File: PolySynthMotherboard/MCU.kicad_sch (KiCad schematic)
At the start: 45 parts, among them J201 SWD Header, J202 USB_C_Leceptacle_USB2.0, J203 MIDI_In, J204 MIDI_Thru, J205 MIDI_Out, J401 Micro_SD_Card_Det2, SW201 RST, SW202 BOOT, U201 STM32F411RETx, U202 74HC595, U203 74HC595, U204 4N35, U205 74HC04, Y201 16MHz, Y202 32.768kHZ

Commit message: power supply tweaks
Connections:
- net BATT_REF: now also U201.14 (PA0); no longer U201.26 (PB0)
- new net DAC_INH: U201.26 (PB0)
- no-connect marks 25 -> 24
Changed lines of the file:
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@@
   (no_connect (at 200.406 137.414))
   (no_connect (at 121.158 55.118))
-  (no_connect (at 121.158 47.498))
   (no_connect (at 185.928 212.852))
   (no_connect (at 121.158 62.738))
@@
   )
   (wire (pts (xy 115.57 31.242) (xy 115.57 32.004))
+    (stroke (width 0) (type default))
+  )
+  (wire (pts (xy 121.158 47.498) (xy 124.714 47.498))
     (stroke (width 0) (type default))
   )
@@
     )
   )
+  (global_label "DAC_INH" (shape output) (at 126.873 90.678 0) (fields_autoplaced)
+    (effects (font (size 1.27 1.27)) (justify left))
+    (property "Intersheetrefs" "${INTERSHEET_REFS}" (at 137.7202 90.678 0)
+      (effects (font (size 1.27 1.27)) (justify left) hide)
+    )
+  )
   (global_label "MIDI_LX" (shape output) (at 384.937 47.244 0) (fields_autoplaced)
     (effects (font (size 1.27 1.27)) (justify left))
@@
     )
   )
-  (global_label "BATT_REF" (shape input) (at 126.873 90.678 0) (fields_autoplaced)
-    (effects (font (size 1.27 1.27)) (justify left))
-    (property "Intersheetrefs" "${INTERSHEET_REFS}" (at 138.6272 90.678 0)
-      (effects (font (size 1.27 1.27)) (justify left) hide)
-    )
+  (global_label "BATT_REF" (shape input) (at 124.714 47.498 0) (fields_autoplaced)
+    (effects (font (size 1.27 1.27)) (justify left))
+    (property "Intersheetrefs" "${INTERSHEET_REFS}" (at 136.4682 47.498 0)
+      (effects (font (size 1.27 1.27)) (justify left) hide)
+    )

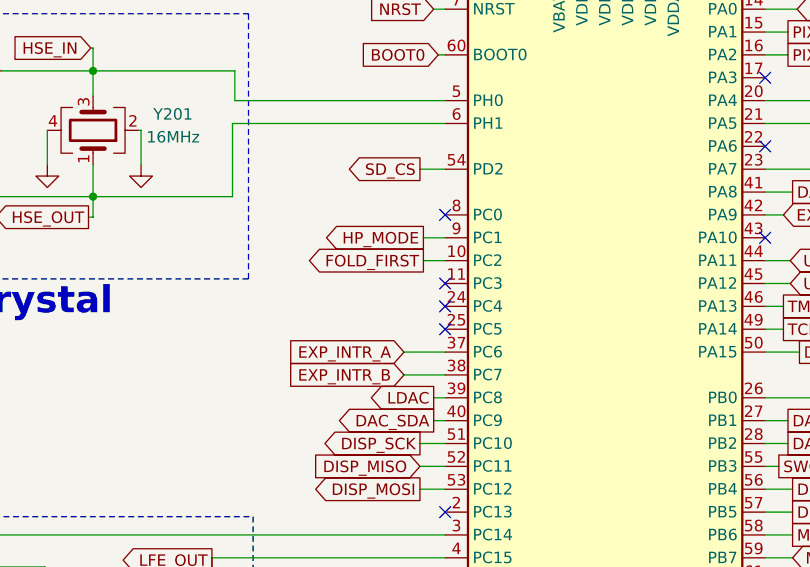
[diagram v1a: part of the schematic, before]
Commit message: cleaned up CV opamps
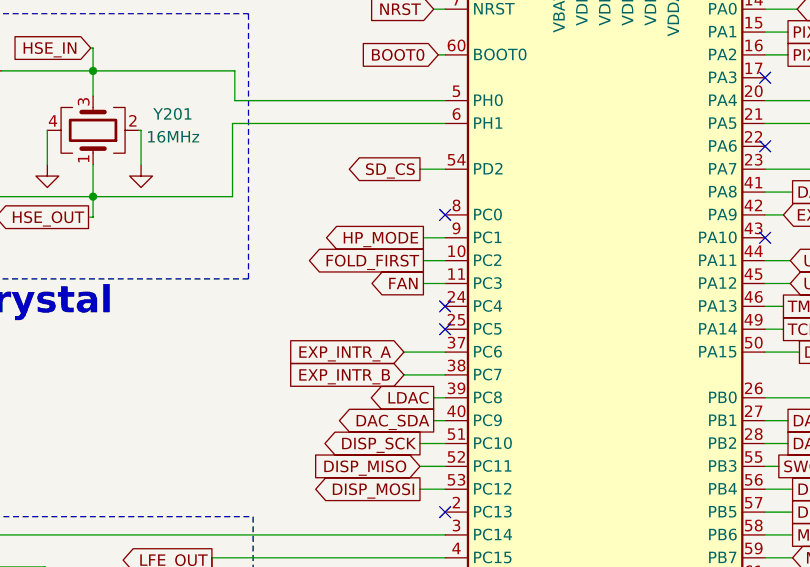
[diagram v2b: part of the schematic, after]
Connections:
- net FAN: now reaches U201.11 (PC3)
- no-connect marks 24 -> 23
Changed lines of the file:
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@@
   (no_connect (at 85.598 70.358))
   (no_connect (at 121.158 72.898))
-  (no_connect (at 85.598 77.978))
   (no_connect (at 279.654 65.659))
   (no_connect (at 85.598 103.378))
@@
     (stroke (width 0) (type default))
   )
+  (wire (pts (xy 83.185 77.978) (xy 85.598 77.978))
+    (stroke (width 0) (type default))
+  )
   (wire (pts (xy 308.102 58.547) (xy 308.102 63.119))
     (stroke (width 0) (type default))
@@
     )
   )
+  (global_label "FAN" (shape output) (at 83.185 77.978 180) (fields_autoplaced)
+    (effects (font (size 1.27 1.27)) (justify right))
+    (property "Intersheetrefs" "${INTERSHEET_REFS}" (at 76.6921 77.978 0)
+      (effects (font (size 1.27 1.27)) (justify right) hide)
+    )
+  )

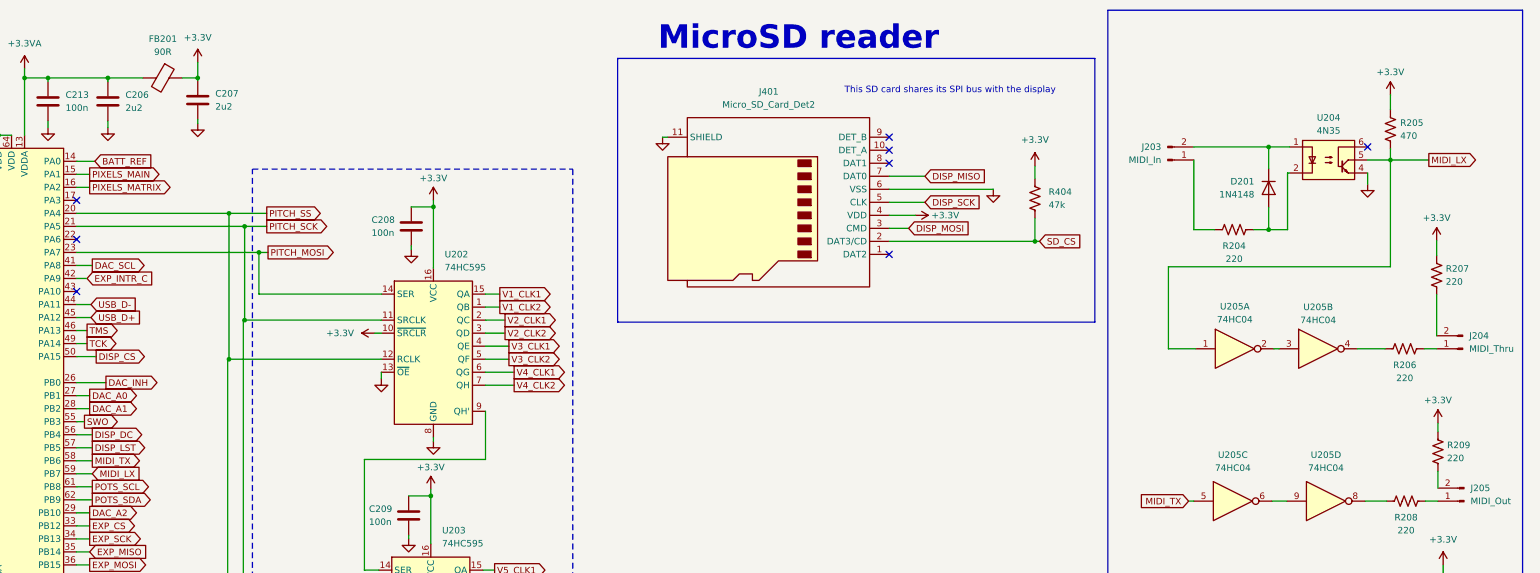
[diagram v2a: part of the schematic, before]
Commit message: footprints placed
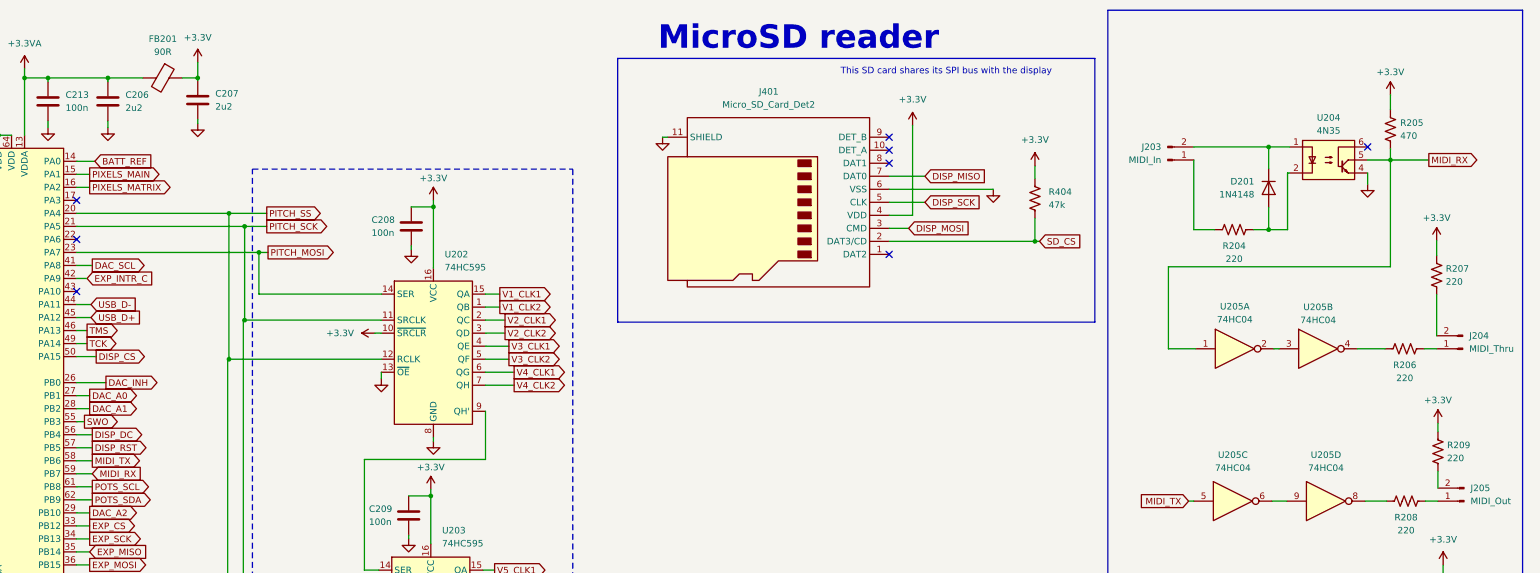
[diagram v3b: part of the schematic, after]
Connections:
- net DISP_LST renamed DISP_RST
- net MIDI_LX renamed MIDI_RX
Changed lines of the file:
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@@
+    (stroke (width 0) (type default))
+  )
+  (wire (pts (xy 284.226 40.513) (xy 284.226 58.039))
     (stroke (width 0) (type default))
   )
@@
     (stroke (width 0) (type default))
   )
+  (wire (pts (xy 284.226 58.039) (xy 279.654 58.039))
+    (stroke (width 0) (type default))
+  )
   (wire (pts (xy 200.914 86.106) (xy 205.486 86.106))
     (stroke (width 0) (type default))
@@
   )
   (wire (pts (xy 190.754 56.388) (xy 190.754 68.326))
-    (stroke (width 0) (type default))
-  )
-  (wire (pts (xy 279.654 58.039) (xy 284.734 58.039))
     (stroke (width 0) (type default))
   )
@@
     (effects (font (size 3 3) (thickness 0.6) bold) (justify left bottom))
   )
-  (text "This SD card shares its SPI bus with the display" (at 312.166 34.417 0)
+  (text "This SD card shares its SPI bus with the display" (at 311.404 30.734 0)
     (effects (font (size 1.27 1.27)) (justify right bottom))
   )
@@
     )
   )
-  (global_label "MIDI_LX" (shape input) (at 124.206 108.458 0) (fields_autoplaced)
+  (global_label "MIDI_RX" (shape input) (at 124.206 108.458 0) (fields_autoplaced)
     (effects (font (size 1.27 1.27)) (justify left))
     (property "Intersheetrefs" "${INTERSHEET_REFS}" (at 134.5693 108.458 0)
@@
     )
   )
-  (global_label "MIDI_LX" (shape output) (at 384.937 47.244 0) (fields_autoplaced)
+  (global_label "MIDI_RX" (shape output) (at 384.937 47.244 0) (fields_autoplaced)
     (effects (font (size 1.27 1.27)) (justify left))
     (property "Intersheetrefs" "${INTERSHEET_REFS}" (at 395.3003 47.244 0)
@@
     )
   )
-  (global_label "DISP_LST" (shape output) (at 124.206 103.378 0) (fields_autoplaced)
+  (global_label "DISP_RST" (shape output) (at 124.206 103.378 0) (fields_autoplaced)
     (effects (font (size 1.27 1.27)) (justify left))
     (property "Intersheetrefs" "${INTERSHEET_REFS}" (at 135.9602 103.378 0)
@@
     )
   )
+  (symbol (lib_id "power:+3.3V") (at 284.226 40.513 0) (unit 1)
+    (in_bom yes) (on_board yes) (dnp no) (fields_autoplaced)
+    (property "Reference" "#PWR0425" (at 284.226 44.323 0)
+      (effects (font (size 1.27 1.27)) hide)
+    )
+    (property "Value" "+3.3V" (at 284.226 35.433 0)
+      (effects (font (size 1.27 1.27)))
+    )
+    (property "Footprint" "" (at 284.226 40.513 0)
+      (effects (font (size 1.27 1.27)) hide)
+    )
+    (property "Datasheet" "" (at 284.226 40.513 0)
+      (effects (font (size 1.27 1.27)) hide)
+    )
+    (pin "1")
+    (instances
+      (project "ESP808_mk3"
+        (path "/1b0f4827-7224-4696-9105-e83073878432/12afefba-537f-4d88-bb0b-d3898664142d"
+          (reference "#PWR0425") (unit 1)
+        )
+      )
+      (project "PolySynthMotherboard"
+        (path "/22649217-9810-470f-bc7b-6f743ad2b90e/30ed774f-a7f6-4caf-bf27-d83abb3db248"
+          (reference "#PWR0249") (unit 1)
+        )
+      )
+      (project "Quadriscope"
+        (path "/b6082534-8496-42f5-914d-c32eba9832ab"
+          (reference "#PWR0164") (unit 1)
+        )
+      )
+      (project "MCU"
+        (path "/dbce208f-32c5-4e57-807b-6eb4ab6aa944"
+          (reference "#PWR0425") (unit 1)
+        )
+      )
+    )
+  )
   (symbol (lib_id "Connector:Micro_SD_Card_Det2") (at 256.794 55.499 180) (unit 1)
     (in_bom yes) (on_board yes) (dnp no) (fields_autoplaced)
@@
         )
       )
-    )
-  )
-  (symbol (lib_id "power:+3.3V") (at 284.734 58.039 270) (unit 1)
-    (in_bom yes) (on_board yes) (dnp no) (fields_autoplaced)
-    (property "Reference" "#PWR0411" (at 280.924 58.039 0)
-      (effects (font (size 1.27 1.27)) hide)
-    )
-    (property "Value" "+3.3V" (at 287.909 58.039 90)
-      (effects (font (size 1.27 1.27)) (justify left))
-    )
-    (property "Footprint" "" (at 284.734 58.039 0)
-      (effects (font (size 1.27 1.27)) hide)
-    )
-    (property "Datasheet" "" (at 284.734 58.039 0)
-      (effects (font (size 1.27 1.27)) hide)
-    )
-    (pin "1")
-    (instances
-      (project "ESP808_mk3"
-        (path "/1b0f4827-7224-4696-9105-e83073878432/12afefba-537f-4d88-bb0b-d3898664142d"
-          (reference "#PWR0411") (unit 1)
-        )
-      )
-      (project "PolySynthMotherboard"
-        (path "/22649217-9810-470f-bc7b-6f743ad2b90e/30ed774f-a7f6-4caf-bf27-d83abb3db248"
-          (reference "#PWR0249") (unit 1)
-        )
-      )
-      (project "Quadriscope"
-        (path "/b6082534-8496-42f5-914d-c32eba9832ab"
-          (reference "#PWR0161") (unit 1)
-        )
-      )
-      (project "DualDigitalVCO"
-        (path "/c34b0bf2-bf4f-4f09-a49d-1acd5b47c7ca"
-          (reference "#PWR0132") (unit 1)
-        )
-        (path "/c34b0bf2-bf4f-4f09-a49d-1acd5b47c7ca/b7b70d81-d74b-4739-995e-589a97e00ba9"
-          (reference "#PWR0340") (unit 1)
-        )
-      )
-      (project "MCU"
-        (path "/dbce208f-32c5-4e57-807b-6eb4ab6aa944"
-          (reference "#PWR0411") (unit 1)
-        )
-      )

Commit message: motherboard rev1
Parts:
- J202: value USB_C_Leceptacle_USB2.0 -> USB_C
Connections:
- net EXP_INTR_A: now also U201.39 (PC8); no longer U201.37 (PC6)
- net EXP_INTR_C: now also U201.37 (PC6); no longer U201.42 (PA9)
- net LDAC: now also U201.42 (PA9); no longer U201.39 (PC8)
- net FAN: no longer names the net of U201.11 (PC3)
- no-connect marks 23 -> 24
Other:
- moved on the sheet: C216, D503, J201, J202, R201, R202, R203, SW201, SW202

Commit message: updated to kicad 8
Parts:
- removed J204: MIDI_Thru, Connector_PinSocket_2.54mm:PinSocket_1x02_P2.54mm_Vertical, symbol Connector:Conn_01x02_Pin
- removed J205: MIDI_Out, Connector_PinSocket_2.54mm:PinSocket_1x02_P2.54mm_Vertical, symbol Connector:Conn_01x02_Pin
- added J204: MIDI_Thru, Connector_PinHeader_2.54mm:PinHeader_1x03_P2.54mm_Vertical, symbol Connector:Conn_01x03_Pin
- added J207: MIDI_Out, Connector_PinHeader_2.54mm:PinHeader_1x03_P2.54mm_Vertical, symbol Connector:Conn_01x03_Pin
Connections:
- net GND: now also J204.2 (Pin_2), J207.2 (Pin_2)
- net at R207.2: now also J204.1 (Pin_1)
- net at R206.1: now also J204.3 (Pin_3)
- net at R209.2: now also J207.1 (Pin_1)
- net at R208.1: now also J207.3 (Pin_3)
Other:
- moved on the sheet: C216, C217, D201, D503, J201, J202, J203, J401, R201, R202, R203, R204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
